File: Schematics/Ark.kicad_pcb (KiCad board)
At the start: 2 copper layers, 71.9 x 89.1 mm, 112 parts, among them P1 USB_OTG, P2 USB_OTG, P3 40_Pin_LCD_Out, P4 6_Pin_Touch_In, P5 CONN_01X01, P6 CONN_01X01, P7 CONN_01X01, Q1 MMUN2133LT1G, SW1 SW_PUSH_SMALL_H, SW2 SW_PUSH_SMALL_H, SW3 SW_PUSH_SMALL_H, SW4 SW_PUSH_SMALL_H, SW5 SW_PUSH_SMALL_H, SW6 SW_PUSH_SMALL_H, U1 PAM2306AYPKE, U2 AP7115-25SEG, U3 DDR2_SODIMM_CM_3_Lite, U4 1040310811, U5 FAN5333BSX, U6 TPS61090RSAR, U7 MCP73871, U8 SPDT_switch

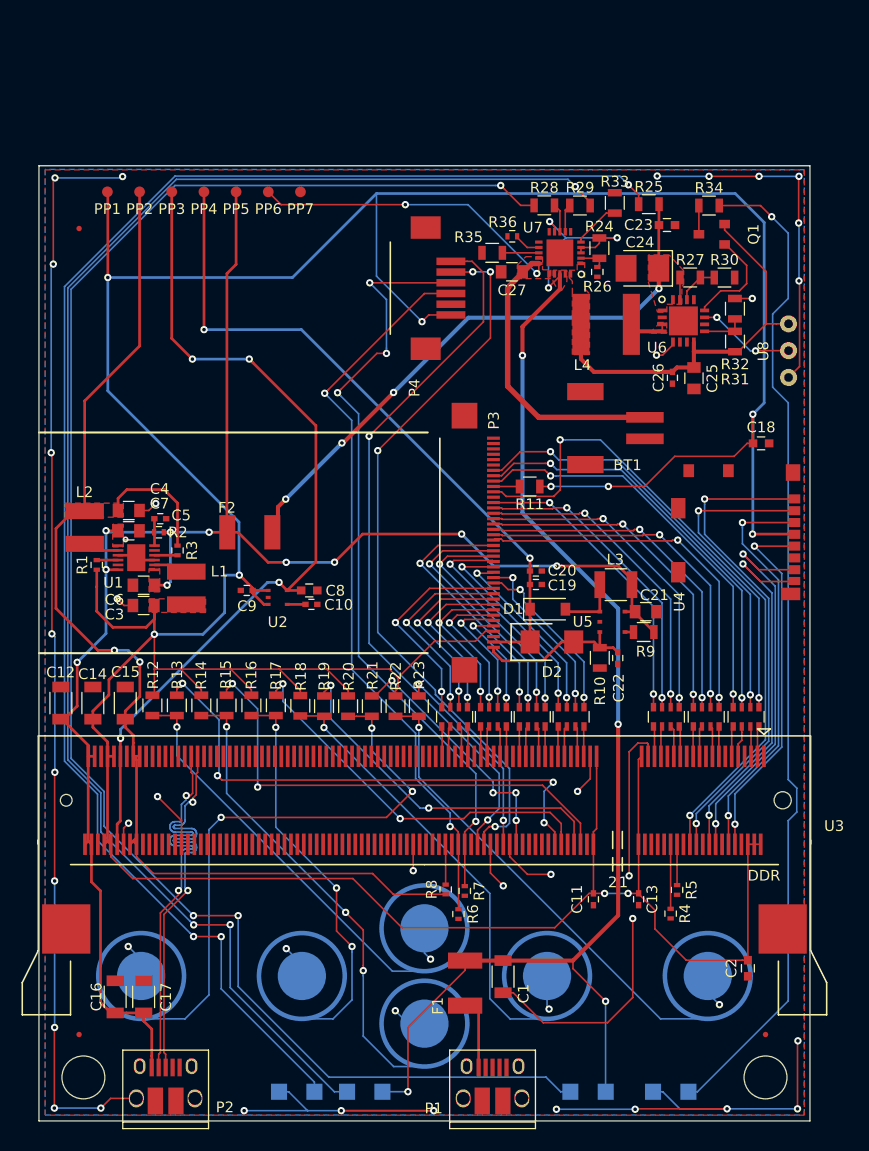
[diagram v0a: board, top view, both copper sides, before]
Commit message: Updated for internal USB
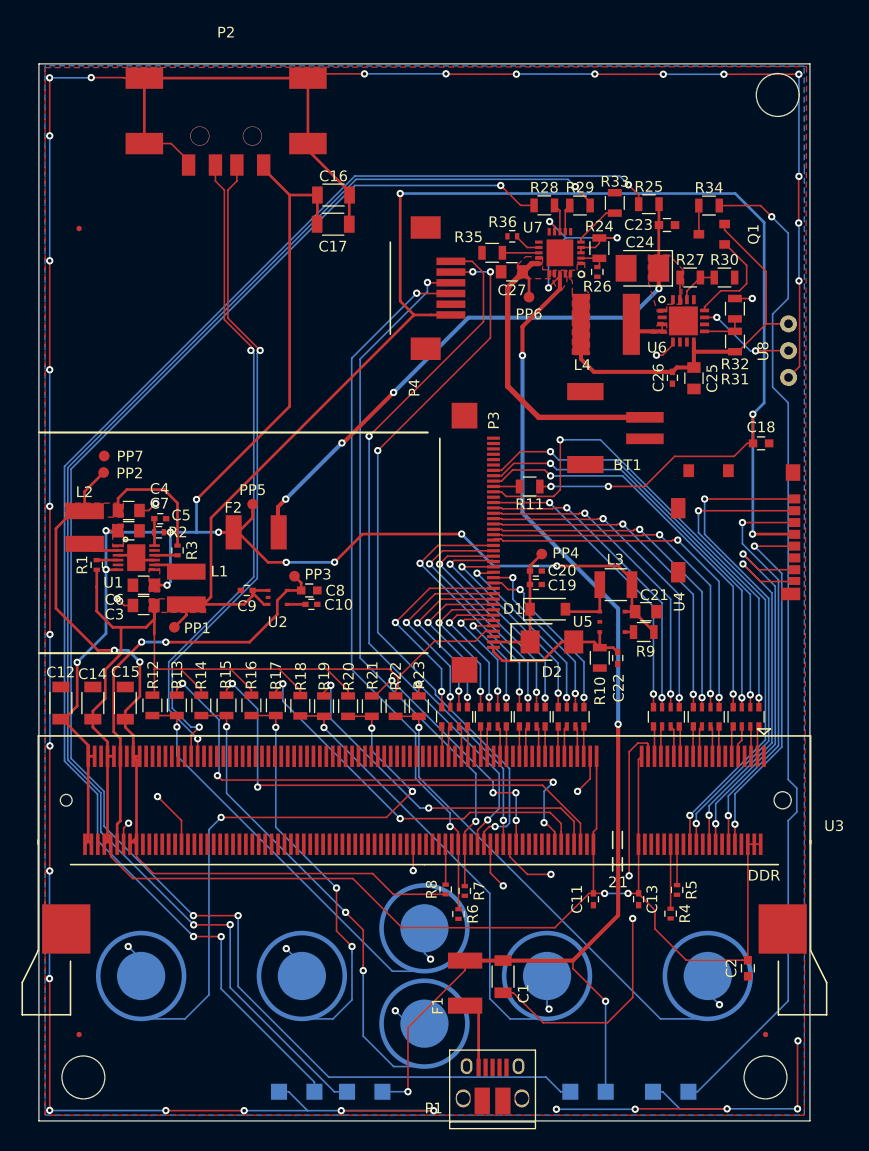
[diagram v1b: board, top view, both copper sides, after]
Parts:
- C22: value 0.1uF -> 100nF
- P2: value USB_OTG -> USB_A; footprint Pi-Library:USB_Micro-B_10103594-0001LF -> Pi-Library:Wurth_USB_732-11179-1-ND
- moved P2 90.9 mm to (121.2, 72.9), turned to 180 degrees
- moved C16 77.5 mm to (131.2, 80.7), turned to 0 degrees
- moved C17 74.2 mm to (131.2, 83.5), turned to 0 degrees
- moved PP4 46.2 mm to (150.6, 114.2)
- moved PP1 41.1 mm to (116.4, 121.0)
- moved PP3 37.6 mm to (127.6, 116.3)
- moved PP7 30.7 mm to (109.8, 105.1)
- moved PP5 29.2 mm to (123.7, 109.6)
- moved PP2 26.4 mm to (109.8, 106.6)
- moved PP6 26.2 mm to (149.4, 90.2)
- moved F2 0.59 mm to (124.0, 112.2)
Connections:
- P2 pad 4: Net-(P2-Pad4) -> GND
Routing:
- net GND: track 290.1 -> 396.1 mm, vias 42 -> 48
- net 24V: track 63.3 -> 12.1 mm, vias 2 -> 0
- net 3V3: track 396.7 -> 355.6 mm, vias 10 -> 7
- net CM_VDAC: track 80.6 -> 39.6 mm, vias 4 -> 2
- net 1V8: track 114.8 -> 87.2 mm
- net Net-(BT1-Pad1): track 56.2 -> 29.6 mm, vias 2 -> 0
- net USB_D-: track 37.9 -> 61.9 mm
- net USB_D+: track 38.1 -> 61.0 mm
- net Net-(D3-Pad2): track 145.6 -> 135.8 mm
- net Net-(D5-Pad1): track 142.6 -> 132.8 mm
- net Net-(D4-Pad1): track 156.9 -> 147.1 mm
- net 5V: track 159.3 -> 149.7 mm, vias 10 -> 11
- net SDA: track 72.7 -> 66.0 mm, vias 4 -> 2
- net SCL: track 69.0 -> 67.4 mm
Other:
- board size 71.9 x 89.1 mm -> 71.9 x 98.6 mm

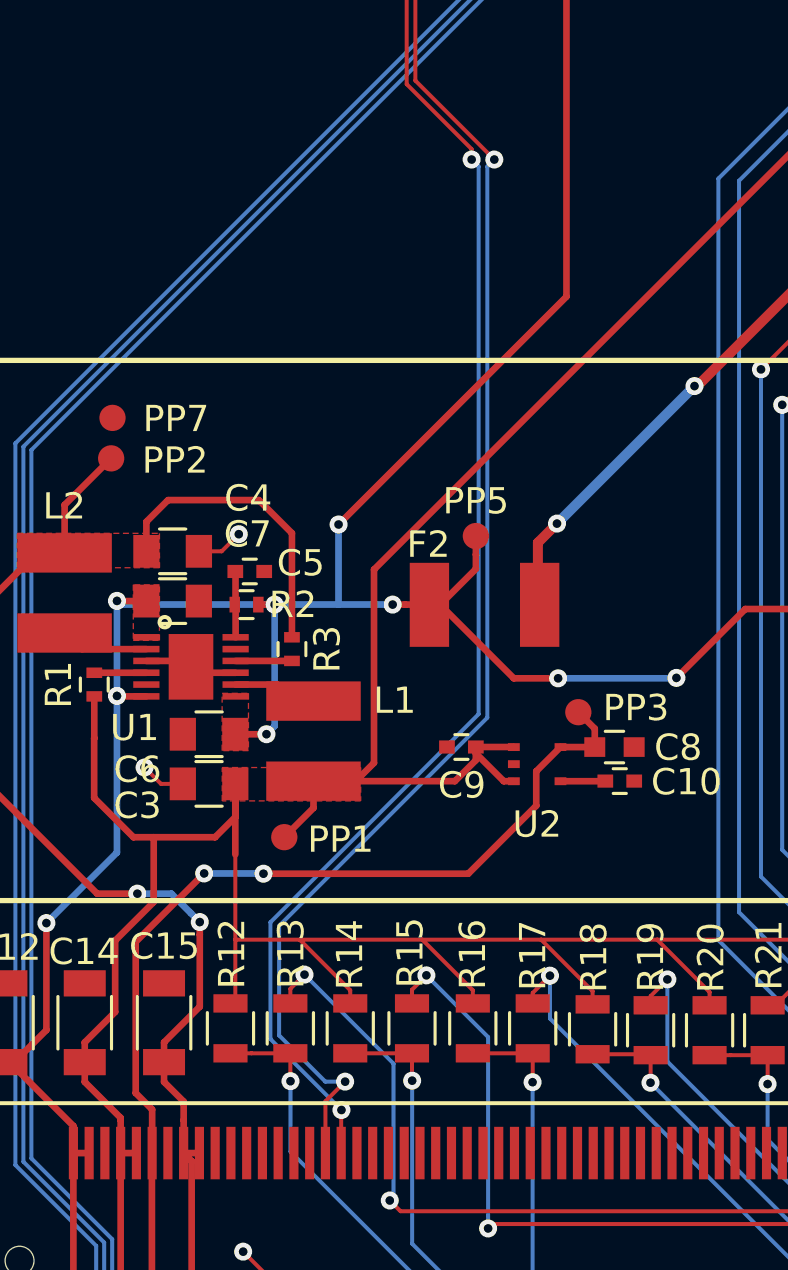
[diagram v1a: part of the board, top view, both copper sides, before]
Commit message: Matched track length on USB
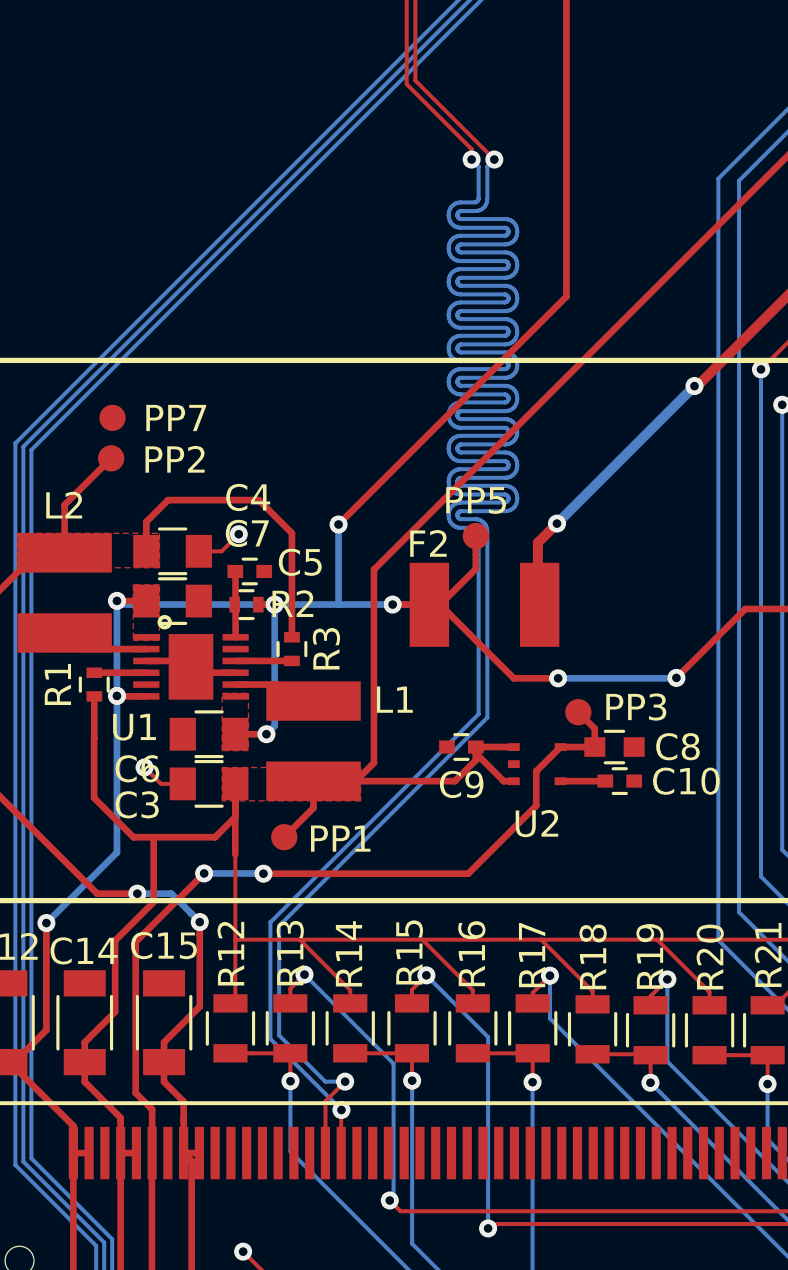
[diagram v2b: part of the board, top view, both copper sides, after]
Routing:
- net USB_D+: track 61.0 -> 99.1 mm
- net USB_D-: track 61.9 -> 100.0 mm
